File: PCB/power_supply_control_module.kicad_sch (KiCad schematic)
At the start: 37 parts, among them J1 ICSP, J2 USB_X, J3 PS_POT, J4 POWER, J5 DISP, J6 USB_Y, J7 USB_A, SW1 Voltage, SW2 Current, SW3 Voltage, SW4 Current, U1 MCP4251-103E-SL, U2 ATmega328PB-A, U3 MCP4251-103E-SL, Y1 Crystal

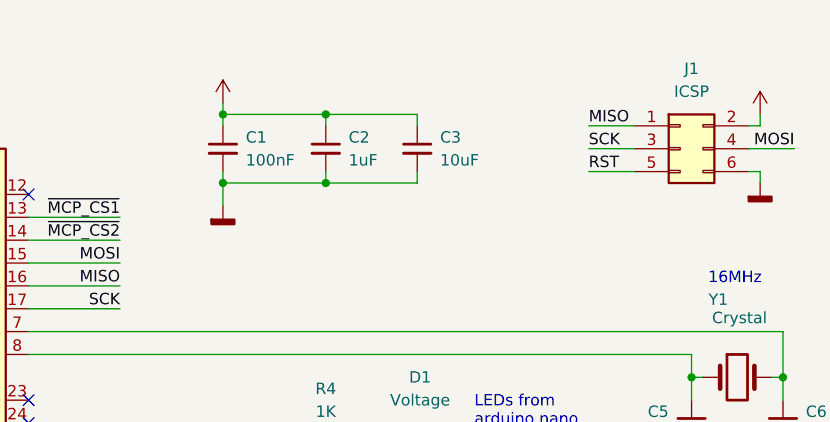
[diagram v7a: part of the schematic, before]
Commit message: added forgotten RST pin treatement
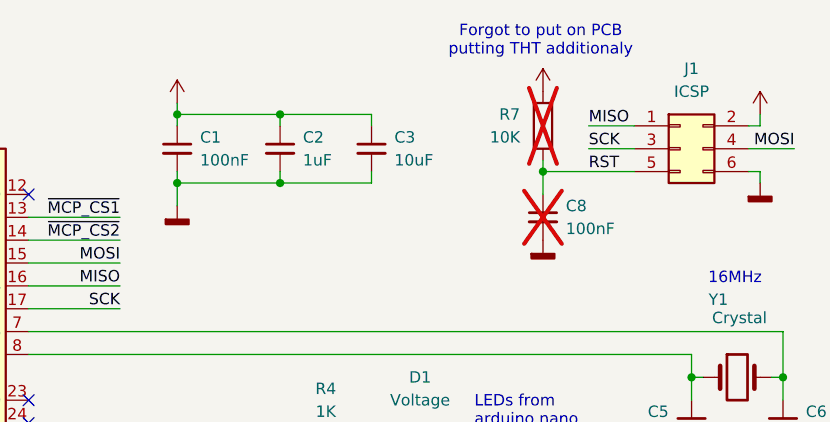
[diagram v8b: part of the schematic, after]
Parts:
- added C8: 100nF, Capacitor_SMD:C_1206_3216Metric_Pad1.33x1.80mm_HandSolder, symbol Device:C_Small
- added R7: 10K, Resistor_SMD:R_1206_3216Metric_Pad1.30x1.75mm_HandSolder, symbol Device:R
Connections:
- net GNDD: now also C8.2
- net RST: now also C8.1, R7.1
- net VCC: now also R7.2
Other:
- note added: "Forgot to put on PCB putting THT additionaly"
- moved on the sheet: C1, C2, C3
